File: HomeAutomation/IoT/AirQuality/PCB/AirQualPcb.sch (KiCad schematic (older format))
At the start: 27 parts, among them J1 Power Switch, J2 QWIIC_CONNECTORJS-1MM, J3 QWIIC_CONNECTORJS-1MM, J4 QWIIC_CONNECTORJS-1MM, J5 UART_CONNECTORJS-1MM, J6 Fan, Q1 BSS138, Q2 BSS138, Q3 BSS138, U1 RP402Nxx1x, U2 Particle_Argon

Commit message: a couple last minute changes before sending to fab
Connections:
- net at J1.3, Q1.3 (D), U2.27 (EN): now also J1.1, Q1.1 (G), R1.2
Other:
- moved on the sheet: C4, Q3
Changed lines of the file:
@@
 	8450 2100 8450 2250
 Wire Wire Line
-	7700 1800 8000 1800
+	7450 1800 8000 1800
 $Comp
 L power:GND #PWR06
@@
 $EndComp
 Wire Wire Line
-	7100 3250 7700 3250
-Wire Wire Line
-	7100 3150 7600 3150
+	7100 3250 7450 3250
+Wire Wire Line
+	7100 3150 7350 3150
 Connection ~ 3500 2200
 Wire Wire Line
@@
 	4650 2750 4700 2750
 Wire Wire Line
-	8450 1600 7600 1600
+	8450 1600 7350 1600
 $Comp
 L Device:C C9
@@
 $EndComp
 Wire Wire Line
-	5050 4750 5050 5300
+	4150 4750 4150 5300
 Connection ~ 5850 5300
 $Comp
@@
 L power:+5V #PWR09
 U 1 1 5FFA77F8
-P 4250 4650
-F 0 "#PWR09" H 4250 4500 50  0001 C CNN
-F 1 "+5V" V 4265 4778 50  0000 L CNN
-F 2 "" H 4250 4650 50  0001 C CNN
-F 3 "" H 4250 4650 50  0001 C CNN
-	1    4250 4650
+P 4350 4650
+F 0 "#PWR09" H 4350 4500 50  0001 C CNN
+F 1 "+5V" V 4365 4778 50  0000 L CNN
+F 2 "" H 4350 4650 50  0001 C CNN
+F 3 "" H 4350 4650 50  0001 C CNN
+	1    4350 4650
 	0    1    1    0
 $EndComp
@@
 L dk_Transistors-FETs-MOSFETs-Single:BSS138 Q3
 U 1 1 5FFAB4C1
-P 4800 4550
-F 0 "Q3" V 4961 4550 60  0000 C CNN
-F 1 "BSS138" V 5067 4550 60  0000 C CNN
-F 2 "digikey-footprints:SOT-23-3" H 5000 4750 60  0001 L CNN
-F 3 "https://www.onsemi.com/pub/Collateral/BSS138-D.PDF" H 5000 4850 60  0001 L CNN
-F 4 "BSS138CT-ND" H 5000 4950 60  0001 L CNN "Digi-Key_PN"
-F 5 "BSS138" H 5000 5050 60  0001 L CNN "MPN"
-F 6 "Discrete Semiconductor Products" H 5000 5150 60  0001 L CNN "Category"
-F 7 "Transistors - FETs, MOSFETs - Single" H 5000 5250 60  0001 L CNN "Family"
-F 8 "https://www.onsemi.com/pub/Collateral/BSS138-D.PDF" H 5000 5350 60  0001 L CNN "DK_Datasheet_Link"
-F 9 "/product-detail/en/on-semiconductor/BSS138/BSS138CT-ND/244294" H 5000 5450 60  0001 L CNN "DK_Detail_Page"
-F 10 "MOSFET N-CH 50V 220MA SOT-23" H 5000 5550 60  0001 L CNN "Description"
-F 11 "ON Semiconductor" H 5000 5650 60  0001 L CNN "Manufacturer"
-F 12 "Active" H 5000 5750 60  0001 L CNN "Status"
-	1    4800 4550
+P 4900 4550
+F 0 "Q3" V 5061 4550 60  0000 C CNN
+F 1 "BSS138" V 5167 4550 60  0000 C CNN
+F 2 "digikey-footprints:SOT-23-3" H 5100 4750 60  0001 L CNN
+F 3 "https://www.onsemi.com/pub/Collateral/BSS138-D.PDF" H 5100 4850 60  0001 L CNN
+F 4 "BSS138CT-ND" H 5100 4950 60  0001 L CNN "Digi-Key_PN"
+F 5 "BSS138" H 5100 5050 60  0001 L CNN "MPN"
+F 6 "Discrete Semiconductor Products" H 5100 5150 60  0001 L CNN "Category"
+F 7 "Transistors - FETs, MOSFETs - Single" H 5100 5250 60  0001 L CNN "Family"
+F 8 "https://www.onsemi.com/pub/Collateral/BSS138-D.PDF" H 5100 5350 60  0001 L CNN "DK_Datasheet_Link"
+F 9 "/product-detail/en/on-semiconductor/BSS138/BSS138CT-ND/244294" H 5100 5450 60  0001 L CNN "DK_Detail_Page"
+F 10 "MOSFET N-CH 50V 220MA SOT-23" H 5100 5550 60  0001 L CNN "Description"
+F 11 "ON Semiconductor" H 5100 5650 60  0001 L CNN "Manufacturer"
+F 12 "Active" H 5100 5750 60  0001 L CNN "Status"
+	1    4900 4550
 	0    -1   1    0
 $EndComp
@@
 	3850 1750 6100 1750
 Wire Wire Line
-	3500 1600 7600 1600
+	3500 1600 7350 1600
 $Comp
 L dk_Transistors-FETs-MOSFETs-Single:BSS138 Q2
@@
 $EndComp
 Wire Wire Line
-	4150 4750 5050 4750
-Wire Wire Line
-	4150 4650 4200 4650
-Wire Wire Line
 	4150 4550 4500 4550
 Wire Wire Line
@@
 Connection ~ 4500 4550
 Wire Wire Line
-	4500 4550 4600 4550
+	4500 4550 4700 4550
 Wire Wire Line
 	4150 4450 4250 4450
@@
 	5950 3950 5950 4150
 Wire Wire Line
-	5950 4550 5000 4550
+	5950 4550 5100 4550
 Wire Wire Line
 	5950 4150 6200 4150
@@
 Connection ~ 5700 3500
 Wire Wire Line
-	4900 4250 4900 3500
-Wire Wire Line
-	4900 3500 5450 3500
+	5000 4250 5000 3500
+Wire Wire Line
+	5000 3500 5450 3500
 Connection ~ 5450 3500
-Wire Wire Line
-	6100 1750 6100 1950
 $Comp
 L Device:C C4
 U 1 1 5FEDDF17
-P 4200 5000
-F 0 "C4" H 4315 5046 50  0000 L CNN
-F 1 "100nF" H 4315 4955 50  0000 L CNN
-F 2 "Capacitors:0603" H 4238 4850 50  0001 C CNN
-F 3 "" H 4200 5000 50  0001 C CNN
-	1    4200 5000
+P 4300 4850
+F 0 "C4" H 4415 4896 50  0000 L CNN
+F 1 "100nF" H 4415 4805 50  0000 L CNN
+F 2 "Capacitors:0603" H 4338 4700 50  0001 C CNN
+F 3 "" H 4300 4850 50  0001 C CNN
+	1    4300 4850
 	1    0    0    -1
 $EndComp
@@
 L power:GND #PWR010
 U 1 1 5FEDEF98
-P 4200 5200
-F 0 "#PWR010" H 4200 4950 50  0001 C CNN
-F 1 "GND" H 4205 5027 50  0000 C CNN
-F 2 "" H 4200 5200 50  0001 C CNN
-F 3 "" H 4200 5200 50  0001 C CNN
-	1    4200 5200
-	1    0    0    -1
-$EndComp
-Wire Wire Line
-	4200 5150 4200 5200
-Wire Wire Line
-	4200 4850 4200 4650
-Connection ~ 4200 4650
-Wire Wire Line
-	4200 4650 4250 4650
+P 4300 5050
+F 0 "#PWR010" H 4300 4800 50  0001 C CNN
+F 1 "GND" H 4305 4877 50  0000 C CNN
+F 2 "" H 4300 5050 50  0001 C CNN
+F 3 "" H 4300 5050 50  0001 C CNN
+	1    4300 5050
+	1    0    0    -1
+$EndComp
+Wire Wire Line
+	4300 5000 4300 5050
 Wire Wire Line
 	6300 5300 6700 5300
@@
 	6300 4800 6700 4800
 Wire Wire Line
-	5050 5300 5850 5300
+	4150 5300 5850 5300
 Wire Wire Line
 	7200 5300 7700 5300
 Wire Wire Line
 	7200 4800 7700 4800
-Connection ~ 7600 1600
-Wire Wire Line
-	7600 1600 7600 3150
-Wire Wire Line
-	7700 1800 7700 3250
-Wire Wire Line
-	8250 1800 8000 1800
-Wire Wire Line
-	8500 2450 8250 2450
-Wire Wire Line
-	8250 2450 8250 1800
+Connection ~ 7350 1600
+Wire Wire Line
+	7350 1600 7350 3150
+Wire Wire Line
+	7450 1800 7450 3250
+Wire Wire Line
+	8300 1800 8000 1800
+Wire Wire Line
+	8500 2450 8300 2450
+Wire Wire Line
+	8300 2450 8300 2250
+Connection ~ 8300 2250
+Wire Wire Line
+	8300 2250 8300 1800
+Wire Wire Line
+	4300 4700 4300 4650
+Wire Wire Line
+	4150 4650 4300 4650
+Wire Wire Line
+	4350 4650 4300 4650
+Connection ~ 4300 4650
+Wire Wire Line
+	6100 1750 6100 2850
 $Comp
 L SparkFun-Connectors:CONN_02 J6
-U 1 1 5FF0A496
-P 6850 1950
-F 0 "J6" H 6622 1905 45  0000 R CNN
-F 1 "Fan" H 6622 1989 45  0000 R CNN
-F 2 "Connectors:1X02" H 6850 2200 20  0001 C CNN
-F 3 "" H 6850 1950 50  0001 C CNN
-F 4 "" H 6600 2100 45  0000 R BNN "Field4"
-	1    6850 1950
+U 1 1 5FFB50BA
+P 8600 2800
+F 0 "J6" H 8372 2755 45  0000 R CNN
+F 1 "Fan" H 8372 2839 45  0000 R CNN
+F 2 "Connectors:1X02" H 8600 3050 20  0001 C CNN
+F 3 "" H 8600 2800 50  0001 C CNN
+F 4 "" H 8350 2950 45  0000 R BNN "Field4"
+	1    8600 2800
 	-1   0    0    1
 $EndComp
-Connection ~ 6100 1950
-Wire Wire Line
-	6100 1950 6100 2850
 $Comp
 L Device:C C10
-U 1 1 5FF1CC9B
-P 6250 2150
-F 0 "C10" H 6365 2196 50  0000 L CNN
-F 1 "1uF" H 6365 2105 50  0000 L CNN
-F 2 "Capacitors:0603" H 6288 2000 50  0001 C CNN
-F 3 "https://www.digikey.com/en/products/detail/GRM188R60J106ME47D/490-3896-1-ND/965938?itemSeq=349211413" H 6250 2150 50  0001 C CNN
-	1    6250 2150
-	1    0    0    -1
-$EndComp
+U 1 1 5FFB50C0
+P 8100 3000
+F 0 "C10" H 8215 3046 50  0000 L CNN
+F 1 "1uF" H 8215 2955 50  0000 L CNN
+F 2 "Capacitors:0603" H 8138 2850 50  0001 C CNN
+F 3 "https://www.digikey.com/en/products/detail/GRM188R60J106ME47D/490-3896-1-ND/965938?itemSeq=349211413" H 8100 3000 50  0001 C CNN
+	1    8100 3000
+	1    0    0    -1
+$EndComp
+Wire Wire Line
+	8500 3150 8500 2900
+Wire Wire Line
+	7950 2800 8100 2800
+Wire Wire Line
+	8100 2850 8100 2800
+Connection ~ 8100 2800
+Wire Wire Line
+	8100 2800 8500 2800
+Text GLabel 7950 2800 0    50   Input ~ 0
+3V3
 $Comp
 L power:GND #PWR0101
-U 1 1 5FF29F68
-P 6450 2350
-F 0 "#PWR0101" H 6450 2100 50  0001 C CNN
-F 1 "GND" H 6455 2177 50  0000 C CNN
-F 2 "" H 6450 2350 50  0001 C CNN
-F 3 "" H 6450 2350 50  0001 C CNN
-	1    6450 2350
-	1    0    0    -1
-$EndComp
-Wire Wire Line
-	6250 2300 6450 2300
-Wire Wire Line
-	6450 2300 6450 2350
-Wire Wire Line
-	6450 2300 6750 2300
-Wire Wire Line
-	6750 2300 6750 2050
-Connection ~ 6450 2300
-Wire Wire Line
-	6100 1950 6250 1950
-Wire Wire Line
-	6250 2000 6250 1950
-Connection ~ 6250 1950
-Wire Wire Line
-	6250 1950 6750 1950
+U 1 1 5FFB50C6
+P 8100 3200
+F 0 "#PWR0101" H 8100 2950 50  0001 C CNN
+F 1 "GND" H 8105 3027 50  0000 C CNN
+F 2 "" H 8100 3200 50  0001 C CNN
+F 3 "" H 8100 3200 50  0001 C CNN
+	1    8100 3200
+	1    0    0    -1
+$EndComp
+Wire Wire Line
+	8100 3150 8500 3150
+Wire Wire Line
+	8100 3150 8100 3200
+Connection ~ 8100 3150
 $EndSCHEMATC

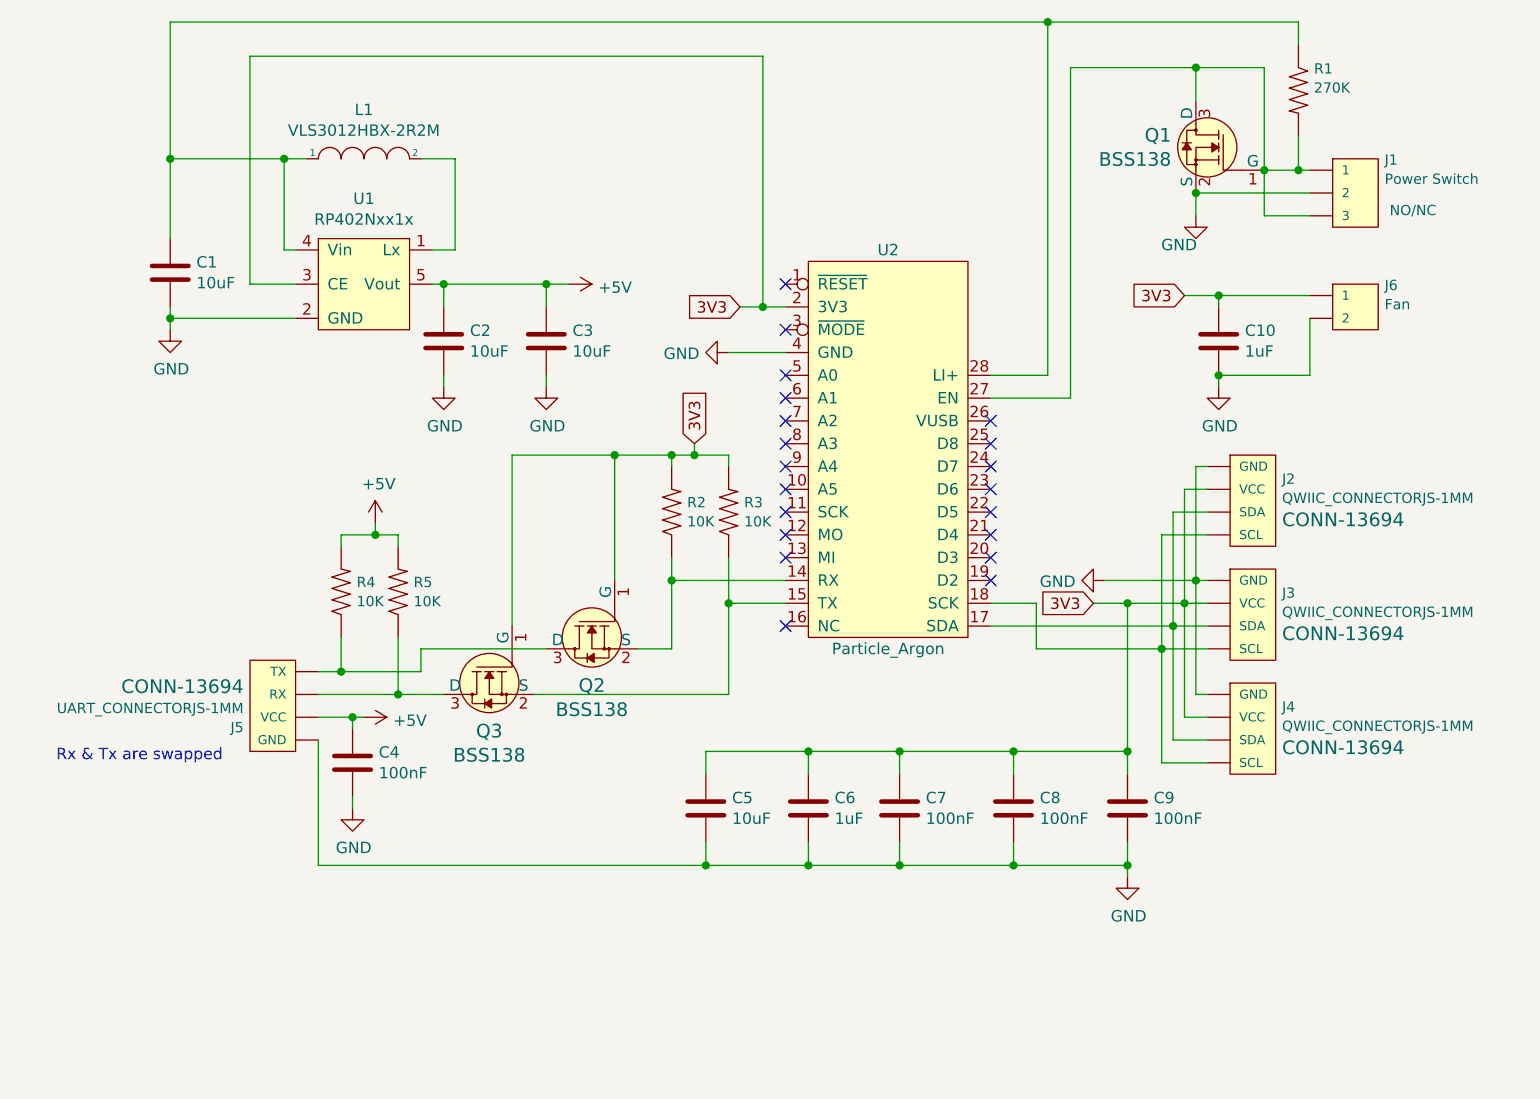
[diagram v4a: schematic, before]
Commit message: PCB: change Argon footprint, direct-connect Sensirion, add button connectors
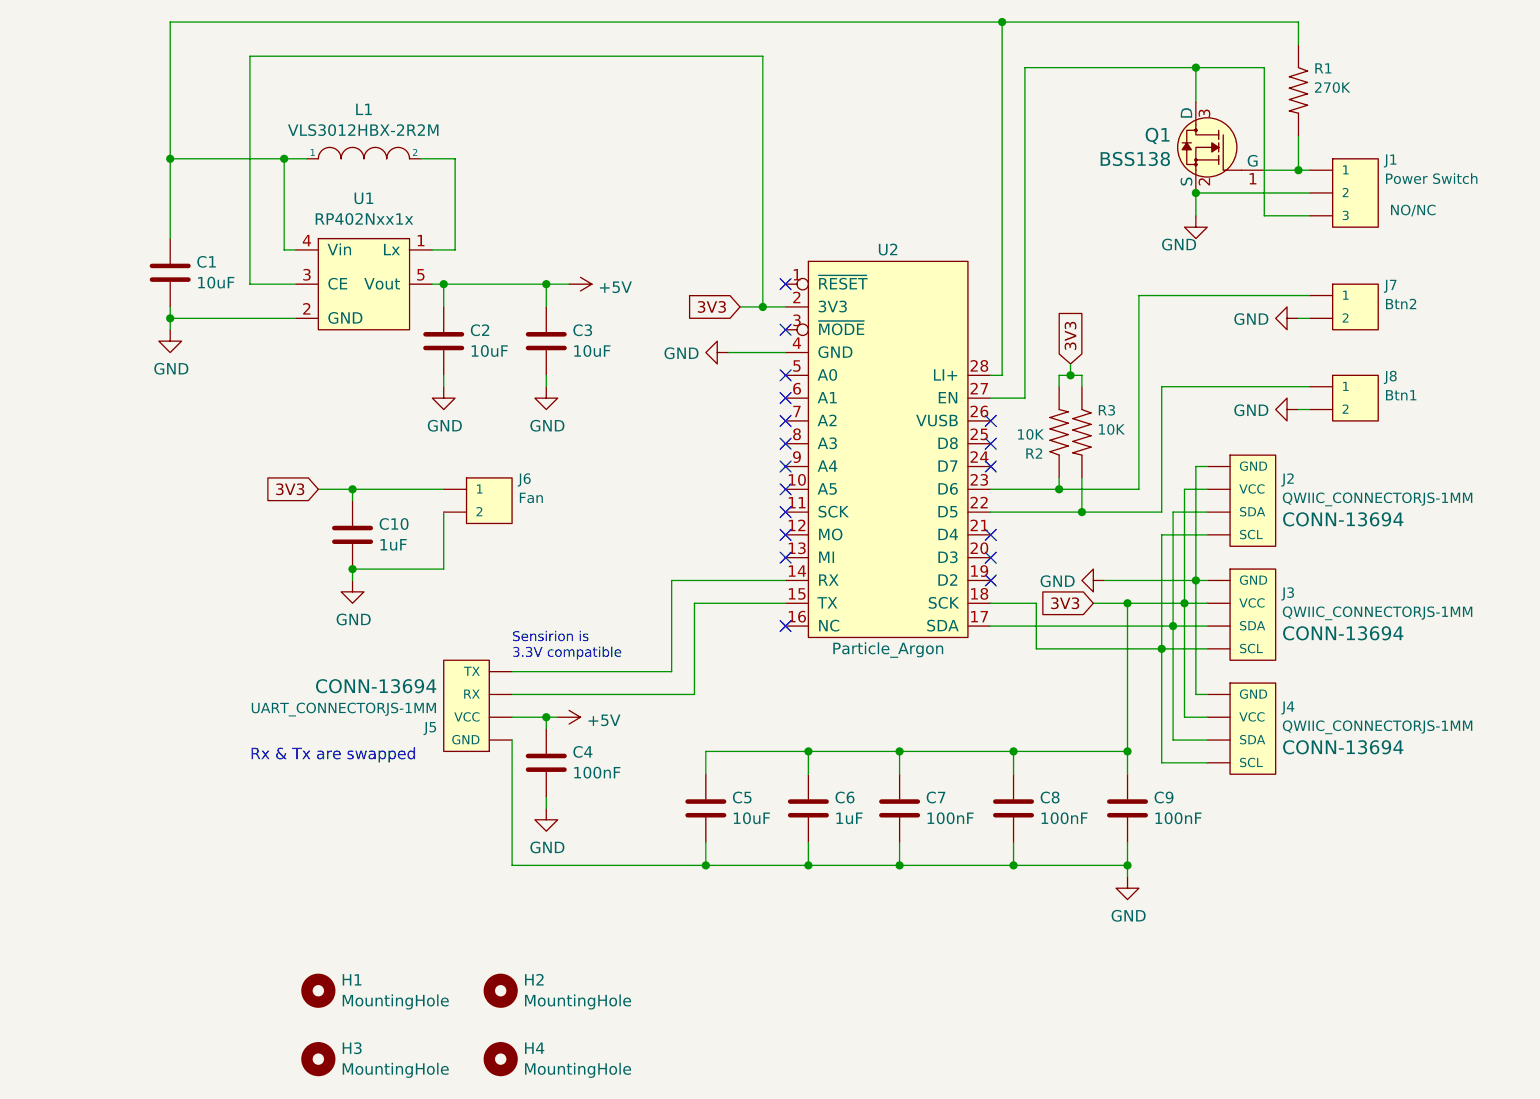
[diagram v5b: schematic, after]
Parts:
- removed Q2, Q3: BSS138, digikey-footprints:SOT-23-3, symbol dk_Transistors-FETs-MOSFETs-Single:BSS138
- removed R4, R5: 10K, 0603, symbol SparkFun-Resistors:RESISTOR0603
- added H1, H2, H3, H4: MountingHole, MountingHole:MountingHole_3.2mm_M3, symbol Mechanical:MountingHole
- added J7: Btn2, Connectors:1X02, symbol SparkFun-Connectors:CONN_02
- added J8: Btn1, Connectors:1X02, symbol SparkFun-Connectors:CONN_02
- R2, R3: footprint 0603 -> Resistor_SMD:R_0603_1608Metric
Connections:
- net 3V3: now also R3.1; no longer R3.2
- net GND: now also J7.2, J8.2
- net at U2.14 (RX): now also J5.4 (TX); no longer R2.1
- net at U2.15 (TX): now also J5.3 (RX); no longer R3.1
- net at U2.22 (D5): now also R3.2, J8.1
- net at U2.23 (D6): now also R2.1, J7.1
- net at J1.3, Q1.3 (D), U2.27 (EN): no longer J1.1, Q1.1 (G), R1.2
- new net: J1.1, Q1.1 (G), R1.2
- no-connect marks 20 -> 18
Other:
- note added: "Sensirion is \n3.3V compatible \n"
- moved on the sheet: C10, C4, J5, J6

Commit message: Fix power supply enable line
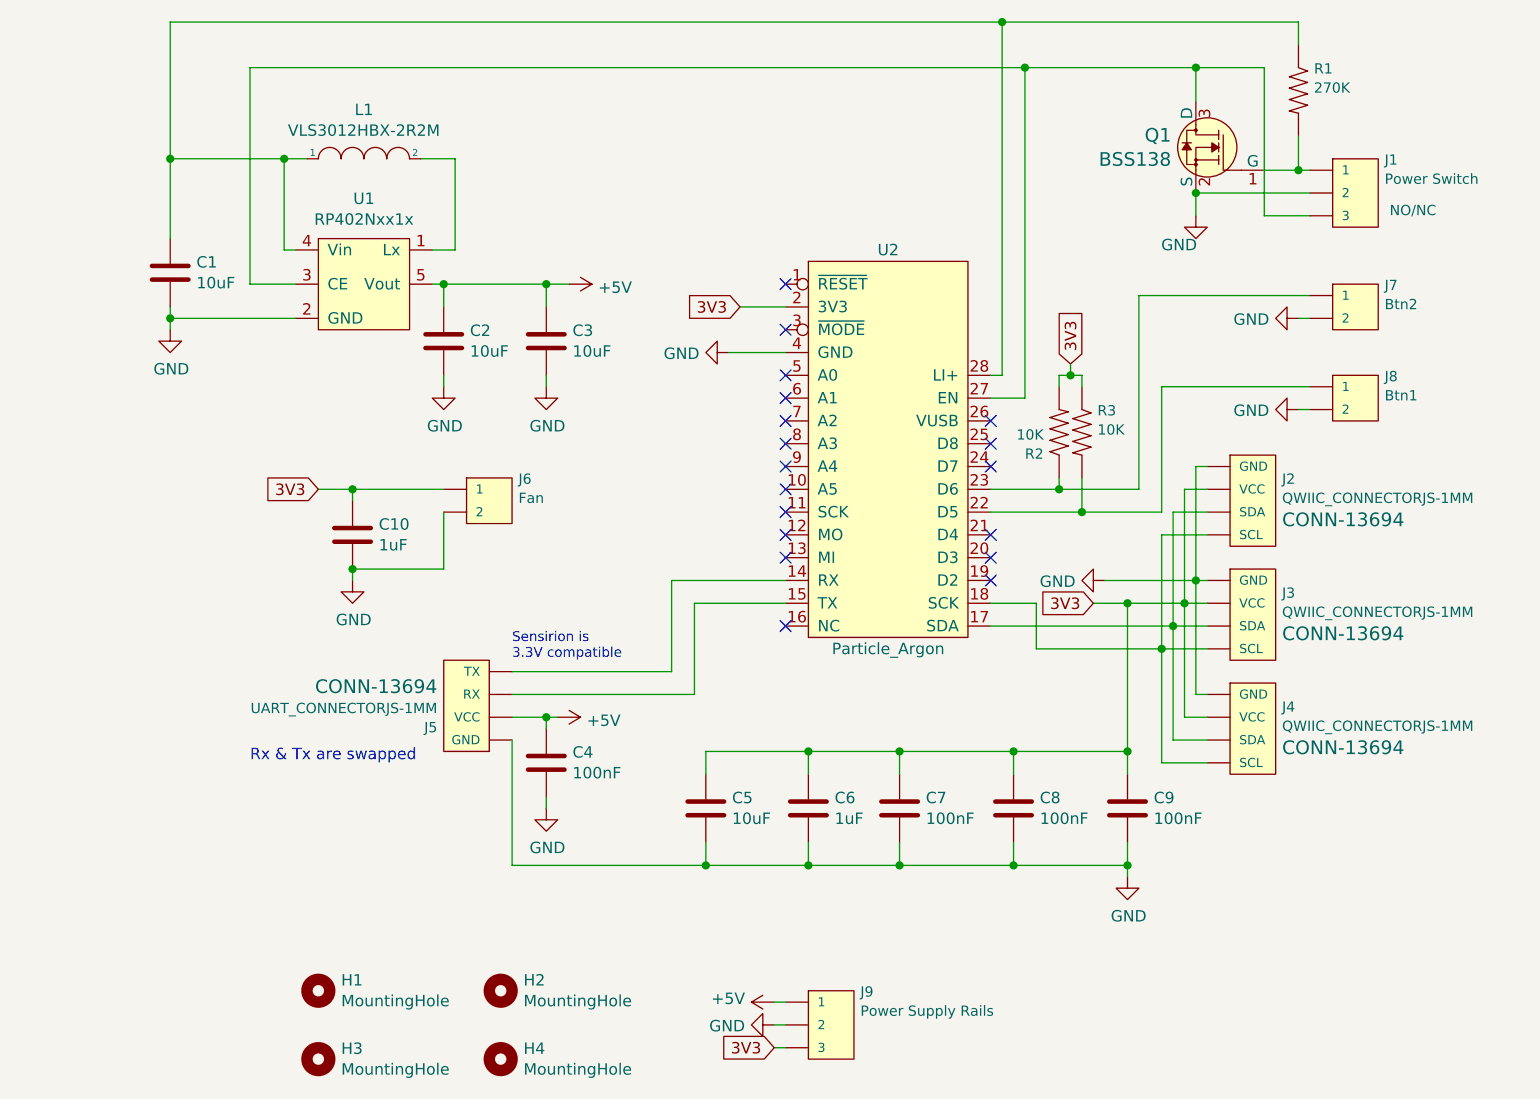
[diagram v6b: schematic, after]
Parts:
- added J9: Power Supply Rails, Connectors:1X03, symbol SparkFun-Connectors:CONN_03
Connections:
- net +5V: now also J9.1
- net 3V3: now also J9.3; no longer U1.3 (CE)
- net GND: now also J9.2
- net at J1.3, Q1.3 (D), U2.27 (EN): now also U1.3 (CE)
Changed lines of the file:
@@
 Text GLabel 6000 2850 0    50   Input ~ 0
 3V3
-Wire Wire Line
-	6200 2850 6100 2850
 $Comp
 L JohnZPCB:Particle_Argon U2
@@
 	4050 2750 3850 2750
 Wire Wire Line
-	3850 2750 3850 1750
-Connection ~ 6100 2850
-Wire Wire Line
-	6100 2850 6000 2850
+	3850 2750 3850 1800
 $Comp
 L Device:C C5
@@
 $EndComp
 Wire Wire Line
-	3850 1750 6100 1750
-Wire Wire Line
 	3500 1600 7150 1600
 Text Notes 3850 4850 0    50   ~ 0
@@
 	5200 4650 5150 4650
 Connection ~ 5150 4650
-Wire Wire Line
-	6100 1750 6100 2850
 $Comp
 L SparkFun-Connectors:CONN_02 J6
@@
 	1    0    0    -1
 $EndComp
+Wire Wire Line
+	6000 2850 6200 2850
+Wire Wire Line
+	7250 1800 3850 1800
+Connection ~ 7250 1800
+$Comp
+L SparkFun-Connectors:CONN_03 J9
+U 1 1 6107E41C
+P 6300 5900
+F 0 "J9" H 6072 5855 45  0000 R CNN
+F 1 "Power Supply Rails" H 6072 5939 45  0000 R CNN
+F 2 "Connectors:1X03" H 6300 6150 20  0001 C CNN
+F 3 "" H 6300 5900 50  0001 C CNN
+F 4 "NO/NC" H 6050 6050 45  0001 R BNN "Field4"
+	1    6300 5900
+	-1   0    0    1
+$EndComp
+$Comp
+L power:GND #PWR0104
+U 1 1 61080786
+P 6150 6000
+F 0 "#PWR0104" H 6150 5750 50  0001 C CNN
+F 1 "GND" V 6155 5872 50  0000 R CNN
+F 2 "" H 6150 6000 50  0001 C CNN
+F 3 "" H 6150 6000 50  0001 C CNN
+	1    6150 6000
+	0    1    1    0
+$EndComp
+Text GLabel 6150 6100 0    50   Input ~ 0
+3V3
+$Comp
+L power:+5V #PWR0105
+U 1 1 610813A9
+P 6150 5900
+F 0 "#PWR0105" H 6150 5750 50  0001 C CNN
+F 1 "+5V" V 6165 6028 50  0000 L CNN
+F 2 "" H 6150 5900 50  0001 C CNN
+F 3 "" H 6150 5900 50  0001 C CNN
+	1    6150 5900
+	0    -1   -1   0
+$EndComp
+Wire Wire Line
+	6150 5900 6200 5900
+Wire Wire Line
+	6200 6000 6150 6000
+Wire Wire Line
+	6150 6100 6200 6100
 $EndSCHEMATC
